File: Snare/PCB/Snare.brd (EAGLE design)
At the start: 100 x 50 mm, 100 parts, among them IC1 LM741P, IC2 LM741P, IC3 LM741P, IC4 LM741P, IC5 LM741P, IC6 LM741P, Q1 2N3904, Q2 2N3904, Q3 2N2222A, Q4 2N2222A, Q6 2N3904

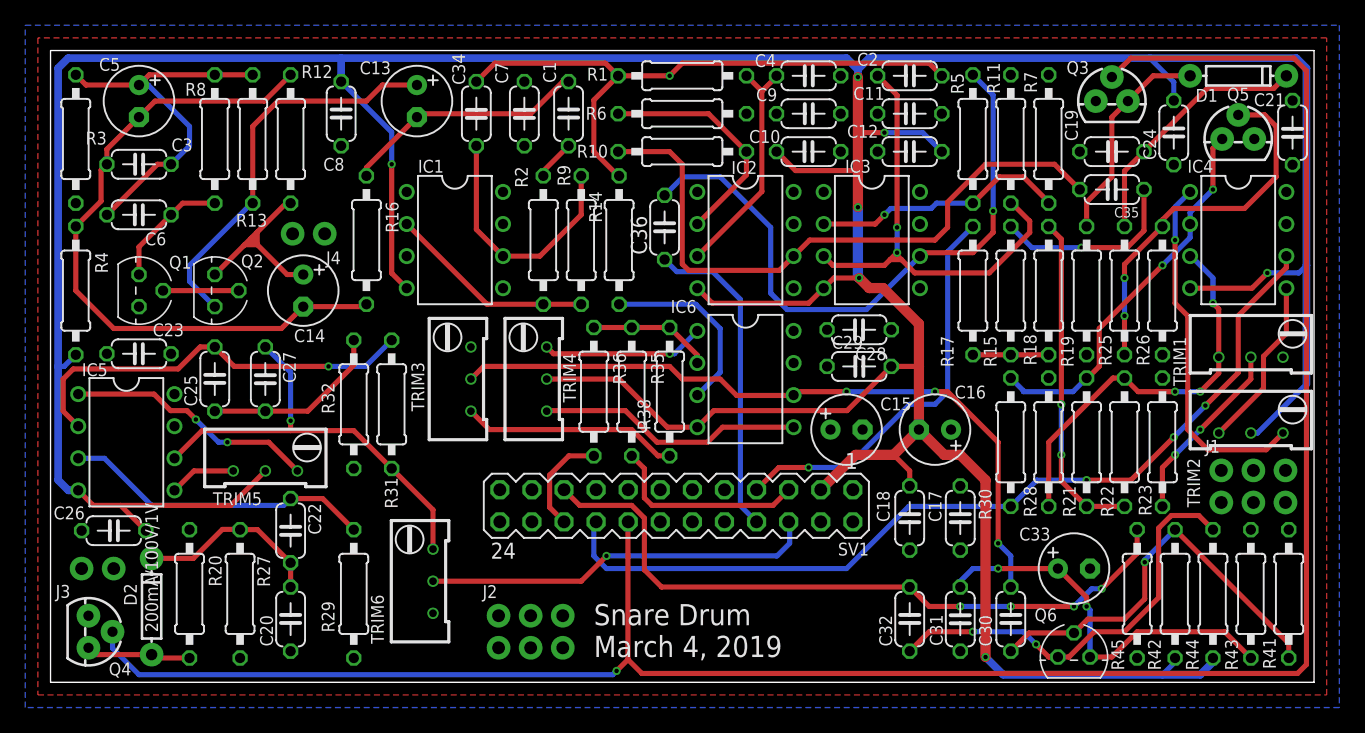
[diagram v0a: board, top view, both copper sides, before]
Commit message: Created Gerbers again and fixed Seeed DRC errors
Created Gerbers again and fixed Seeed DRC errors
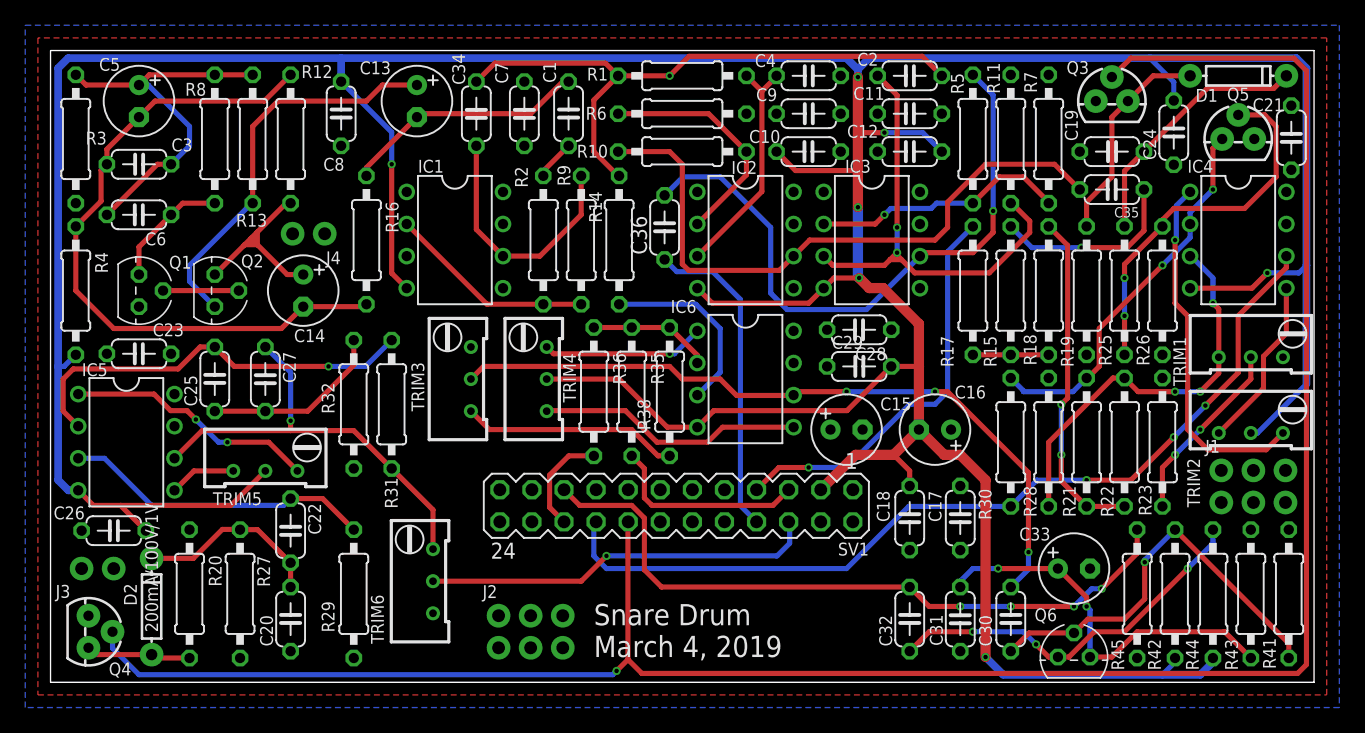
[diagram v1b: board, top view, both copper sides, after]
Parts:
- moved C21 0.41 mm to (98.2, 43.1)
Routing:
- net N$38: track 33.8 -> 30.3 mm, vias 2 -> 3
- net CC_INPUT: track 56.8 -> 57.9 mm
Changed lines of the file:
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@@
 </class>
 </classes>
-<designrules name="JLCPCB2Layer">
+<designrules name="SeeedStudio_2layer_DRU_no_angle_20140221">
 <description language="de">&lt;b&gt;EAGLE Design Rules&lt;/b&gt;
 &lt;p&gt;
@@
 </description>
 <param name="layerSetup" value="(1*16)"/>
-<param name="mtCopper" value="0.035mm 0.035mm 0.035mm 0.035mm 0.035mm 0.035mm 0.035mm 0.035mm 0.035mm 0.035mm 0.035mm 0.035mm 0.035mm 0.035mm 0.035mm 0.035mm"/>
-<param name="mtIsolate" value="1.5mm 0.15mm 0.2mm 0.15mm 0.2mm 0.15mm 0.2mm 0.15mm 0.2mm 0.15mm 0.2mm 0.15mm 0.2mm 0.15mm 0.2mm"/>
+<param name="mtCopper" value="0.035mm 0.0175mm 0.035mm 0.035mm 0.035mm 0.035mm 0.035mm 0.035mm 0.035mm 0.035mm 0.035mm 0.035mm 0.035mm 0.035mm 0.0175mm 0.035mm"/>
+<param name="mtIsolate" value="1.5mm 1.1mm 0.2mm 0.15mm 0.2mm 0.15mm 0.2mm 0.15mm 0.2mm 0.15mm 0.2mm 0.15mm 0.2mm 0.15mm 0.2mm"/>
 <param name="mdWireWire" value="6mil"/>
 <param name="mdWirePad" value="6mil"/>
@@
 <param name="mdSmdStop" value="0mil"/>
 <param name="msWidth" value="6mil"/>
-<param name="msDrill" value="10mil"/>
-<param name="msMicroVia" value="10mil"/>
+<param name="msDrill" value="12mil"/>
+<param name="msMicroVia" value="12mil"/>
 <param name="msBlindViaRatio" value="0.5"/>
 <param name="rvPadTop" value="0.25"/>
@@
 <param name="rvMicroViaOuter" value="0.25"/>
 <param name="rvMicroViaInner" value="0.25"/>
-<param name="rlMinPadTop" value="6mil"/>
+<param name="rlMinPadTop" value="10mil"/>
 <param name="rlMaxPadTop" value="20mil"/>
-<param name="rlMinPadInner" value="6mil"/>
+<param name="rlMinPadInner" value="10mil"/>
 <param name="rlMaxPadInner" value="20mil"/>
-<param name="rlMinPadBottom" value="6mil"/>
+<param name="rlMinPadBottom" value="10mil"/>
 <param name="rlMaxPadBottom" value="20mil"/>
 <param name="rlMinViaOuter" value="6mil"/>
@@
 <attribute name="VALUE" x="91.567" y="41.341" size="1.27" layer="27" ratio="10" rot="R90"/>
 </element>
-<element name="C21" library="resistor" library_urn="urn:adsk.eagle:library:348" package="C050-024X044" package3d_urn="urn:adsk.eagle:package:26162/1" value="0.1uF" x="98.3" y="43.5" smashed="yes" rot="R270">
-<attribute name="NAME" x="95.241" y="45.597" size="1.016" layer="25" ratio="10"/>
-<attribute name="VALUE" x="95.633" y="45.659" size="1.27" layer="27" ratio="10" rot="R270"/>
+<element name="C21" library="resistor" library_urn="urn:adsk.eagle:library:348" package="C050-024X044" package3d_urn="urn:adsk.eagle:package:26162/1" value="0.1uF" x="98.2" y="43.1" smashed="yes" rot="R270">
+<attribute name="NAME" x="95.141" y="45.197" size="1.016" layer="25" ratio="10"/>
+<attribute name="VALUE" x="95.533" y="45.259" size="1.27" layer="27" ratio="10" rot="R270"/>
 </element>
 <element name="TRIM2" library="rcl" library_urn="urn:adsk.eagle:library:334" package="RTRIM64W" package3d_urn="urn:adsk.eagle:package:23748/1" value="10k" x="95" y="21" smashed="yes" rot="R270">
@@
 <contactref element="R1" pad="1"/>
 <via x="49" y="48" extent="1-16" drill="0.35"/>
-<wire x1="49" y1="48" x2="50" y2="49" width="0.4064" layer="1"/>
-<wire x1="50" y1="49" x2="69.54" y2="49" width="0.4064" layer="1"/>
-<wire x1="69.54" y1="49" x2="70.54" y2="48" width="0.4064" layer="1"/>
 <contactref element="C34" pad="1"/>
 <contactref element="R14" pad="1"/>
@@
 <wire x1="43" y1="42" x2="44.92" y2="40.08" width="0.4064" layer="1"/>
 <wire x1="44.92" y1="40.08" x2="45" y2="40.08" width="0.4064" layer="1"/>
+<wire x1="49" y1="48" x2="50.5428" y2="49.5428" width="0.4064" layer="1"/>
+<wire x1="50.5428" y1="49.5428" x2="68.9972" y2="49.5428" width="0.4064" layer="1"/>
+<wire x1="68.9972" y1="49.5428" x2="70.54" y2="48" width="0.4064" layer="1"/>
 </signal>
 <signal name="N$28">
@@
 <contactref element="Q6" pad="3"/>
 <contactref element="C32" pad="1"/>
-<wire x1="92" y1="12.08" x2="90.88" y2="13.2" width="0.4064" layer="1"/>
-<wire x1="88.7" y1="13.2" x2="87.7" y2="12.2" width="0.4064" layer="1"/>
-<wire x1="87.7" y1="12.2" x2="87.7" y2="6.7" width="0.4064" layer="1"/>
-<wire x1="87.7" y1="6.7" x2="85" y2="4" width="0.4064" layer="1"/>
-<wire x1="85" y1="4" x2="82.6" y2="4" width="0.4064" layer="1"/>
+<wire x1="82.6" y1="4" x2="85" y2="4" width="0.4064" layer="1"/>
 <wire x1="80.6" y1="2" x2="79.73" y2="2" width="0.4064" layer="1"/>
-<wire x1="90.88" y1="13.2" x2="88.7" y2="13.2" width="0.4064" layer="1"/>
 <wire x1="82.6" y1="4" x2="80.6" y2="2" width="0.4064" layer="1"/>
 <wire x1="79.73" y1="2" x2="79" y2="2" width="0.4064" layer="1"/>
@@
 <wire x1="73" y1="4" x2="69.54" y2="4" width="0.4064" layer="1"/>
 <wire x1="69.54" y1="4" x2="68" y2="2.46" width="0.4064" layer="1"/>
+<wire x1="85" y1="4" x2="90" y2="9" width="0.4064" layer="1"/>
+<via x="90" y="9" extent="1-16" drill="0.35"/>
+<wire x1="90" y1="9" x2="92" y2="11" width="0.4064" layer="16"/>
+<wire x1="92" y1="11" x2="92" y2="12.08" width="0.4064" layer="16"/>
 </signal>
 <signal name="N$39">
@@
 <contactref element="IC4" pad="1"/>
 <contactref element="TRIM2" pad="3"/>
-<wire x1="90.19" y1="38.81" x2="89" y2="37.62" width="0.4064" layer="16"/>
-<wire x1="89" y1="37.62" x2="89" y2="35" width="0.4064" layer="16"/>
 <via x="89" y="35" extent="1-16" drill="0.35"/>
 <wire x1="89" y1="35" x2="89" y2="30" width="0.4064" layer="1"/>
@@
 <wire x1="90" y1="20" x2="91.6" y2="18.4" width="0.4064" layer="1"/>
 <wire x1="91.6" y1="18.4" x2="96.21" y2="18.4" width="0.4064" layer="1"/>
+<wire x1="89" y1="35" x2="89.1" y2="35.1" width="0.4064" layer="16"/>
+<wire x1="89.1" y1="37.72" x2="90.19" y2="38.81" width="0.4064" layer="16"/>
+<wire x1="89.1" y1="35.1" x2="89.1" y2="37.72" width="0.4064" layer="16"/>
 </signal>
 <signal name="N$42">
@@
 <contactref element="R22" pad="2"/>
 <wire x1="82" y1="13.92" x2="85" y2="13.92" width="0.4064" layer="1"/>
-<wire x1="79" y1="36.08" x2="80" y2="35.08" width="0.4064" layer="1"/>
-<wire x1="80" y1="35.08" x2="80" y2="22" width="0.4064" layer="1"/>
 <via x="80" y="22" extent="1-16" drill="0.35"/>
 <wire x1="80" y1="22" x2="80" y2="18" width="0.4064" layer="16"/>
@@
 <wire x1="80" y1="18" x2="80" y2="15.92" width="0.4064" layer="1"/>
 <wire x1="80" y1="15.92" x2="82" y2="13.92" width="0.4064" layer="1"/>
+<wire x1="80" y1="22" x2="80.5" y2="22.5" width="0.4064" layer="1"/>
+<wire x1="80.5" y1="22.5" x2="80.5" y2="34.58" width="0.4064" layer="1"/>
+<wire x1="80.5" y1="34.58" x2="79" y2="36.08" width="0.4064" layer="1"/>
 </signal>
 <signal name="CC_INPUT">
@@
 <contactref element="IC6" pad="6"/>
 <contactref element="TRIM3" pad="2"/>
-<wire x1="58.81" y1="22.73" x2="59.04" y2="22.96" width="0.4064" layer="1"/>
-<wire x1="59.04" y1="22.96" x2="59.08" y2="23" width="0.4064" layer="1"/>
+<wire x1="58.81" y1="22.73" x2="59.08" y2="23" width="0.4064" layer="1"/>
 <wire x1="59.08" y1="23" x2="63" y2="23" width="0.4064" layer="1"/>
 <via x="63" y="23" extent="1-16" drill="0.35"/>
@@
 <via x="70" y="23" extent="1-16" drill="0.35"/>
 <wire x1="70" y1="23" x2="71" y2="23" width="0.4064" layer="1"/>
-<wire x1="75" y1="19" x2="75" y2="11" width="0.4064" layer="1"/>
-<via x="75" y="11" extent="1-16" drill="0.35"/>
-<wire x1="75" y1="11" x2="76" y2="10" width="0.4064" layer="16"/>
-<wire x1="76" y1="10" x2="76" y2="7.54" width="0.4064" layer="16"/>
-<wire x1="71" y1="23" x2="75" y2="19" width="0.4064" layer="1"/>
 <wire x1="33.27" y1="24" x2="34.27" y2="25" width="0.4064" layer="1"/>
 <wire x1="34.27" y1="25" x2="49" y2="25" width="0.4064" layer="1"/>
@@
 <wire x1="58.78" y1="22.7" x2="58.81" y2="22.73" width="0.4064" layer="1"/>
 <wire x1="54.3" y1="22.7" x2="58.78" y2="22.7" width="0.4064" layer="1"/>
+<via x="77.4" y="10.3" extent="1-16" drill="0.35"/>
+<wire x1="77.4" y1="10.3" x2="77.4" y2="8.94" width="0.4064" layer="16"/>
+<wire x1="77.4" y1="8.94" x2="76" y2="7.54" width="0.4064" layer="16"/>
+<wire x1="71" y1="23" x2="77.4" y2="16.6" width="0.4064" layer="1"/>
+<wire x1="77.4" y1="16.6" x2="77.4" y2="10.3" width="0.4064" layer="1"/>
 </signal>
 <signal name="N$2">

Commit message: Made a change to the schematic
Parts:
- Q5: value (none) -> J176
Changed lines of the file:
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@@
 <attribute name="VALUE" x="90.05" y="16.65" size="1.27" layer="27"/>
 </element>
-<element name="Q5" library="Capstone" package="TO-92" value="" x="94" y="43" smashed="yes">
+<element name="Q5" library="Capstone" package="TO-92" value="J176" x="94" y="43" smashed="yes">
 <attribute name="NAME" x="94" y="46.048" size="1.016" layer="25" font="vector" ratio="20" align="bottom-center"/>
 </element>
